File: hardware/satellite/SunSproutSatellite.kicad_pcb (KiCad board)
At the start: 4 copper layers, 27.2 x 51.1 mm, 36 parts, among them J1 RJHSE5380_QwiicBusCompatible, J2 Conn_01x03, J3 Conn_01x03, J4 Conn_01x03, J5 Conn_01x03, J6 Conn_01x03, J7 Conn_01x04, J8 Qwiic, U1 PCA9615DPZ, U2 ADS1115IDGS, U3 DS2482S-100+, U4 USBLC6-4SC6

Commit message: fix(satellite): Consolidate shared libraries, fix MDX/links, and update JST PA LCSC part (#24)
* Consolidate Hub and Satellite libraries into shared hardware/libraries

* Add SunSprout logo to Satellite silkscreen and refresh documentation assets

* Fix MDX compilation error and broken links in satellite documentation

* Update DS18B20 and moisture probe connectors to JST PA with LCSC part C131339
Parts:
- added G***: LOGO, project:Logo, B.Cu at (122.1, 113.2)
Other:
- board text added: "SunSproutSatellite REV ${REV_NUM}(${VCSSHORTHASH})"

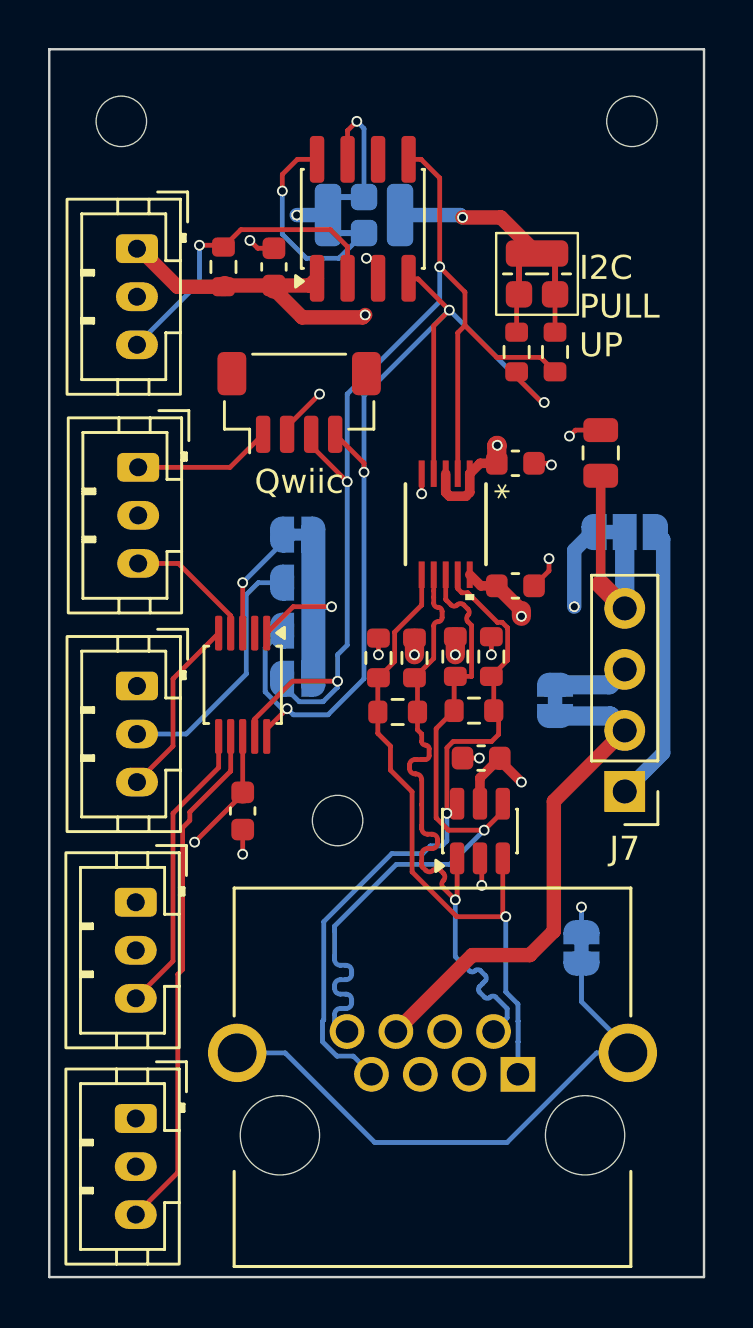
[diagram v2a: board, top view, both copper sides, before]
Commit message: feat(hardware): complete satellite pcb routing and layout review fixes
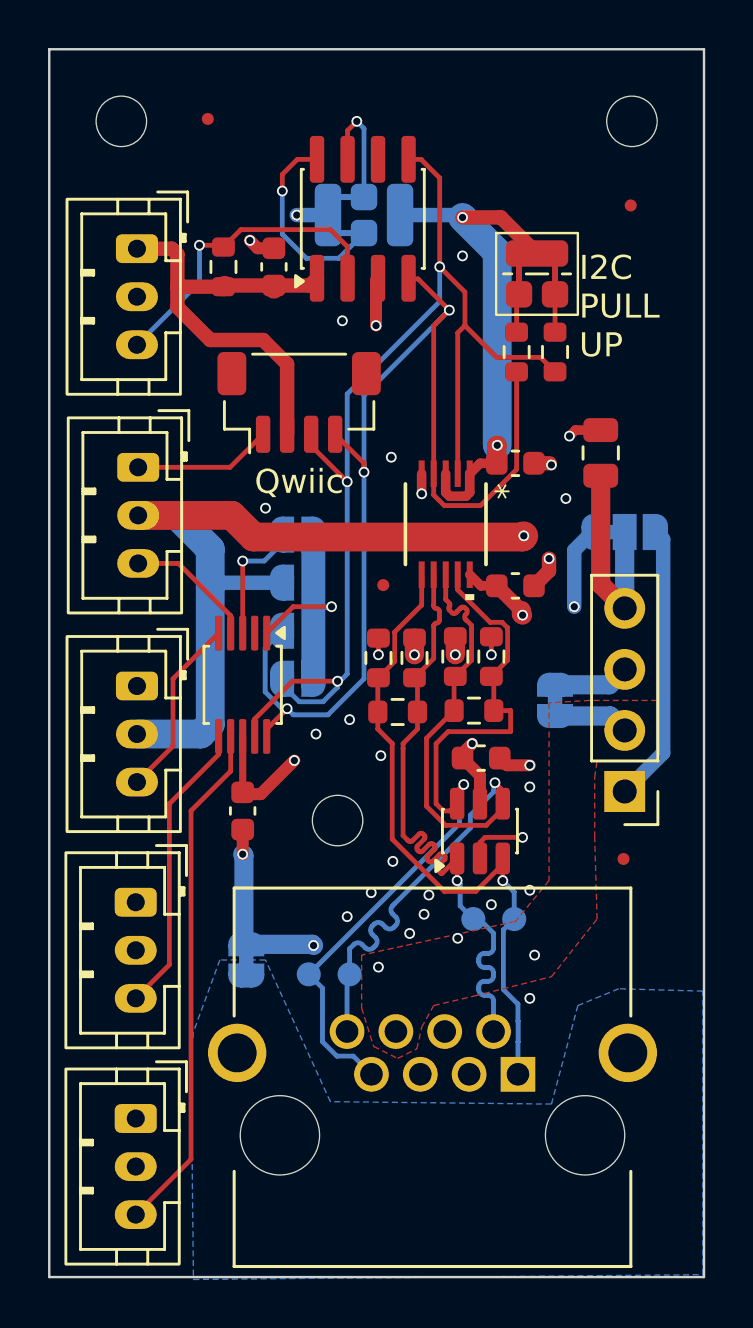
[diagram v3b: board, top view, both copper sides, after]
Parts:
- added Ref**: Fiducial_0.5mm_Mask1mm, PCM_SparkFun-Aesthetic:Fiducial_0.5mm_Mask1mm, F.Cu at (113.9, 122.3)
- added Ref**: Fiducial_0.5mm_Mask1mm, PCM_SparkFun-Aesthetic:Fiducial_0.5mm_Mask1mm, F.Cu at (106.6, 102.9)
- added Ref**: Fiducial_0.5mm_Mask1mm, PCM_SparkFun-Aesthetic:Fiducial_0.5mm_Mask1mm, F.Cu at (123.9, 133.7)
- added Ref**: Fiducial_0.5mm_Mask1mm, PCM_SparkFun-Aesthetic:Fiducial_0.5mm_Mask1mm, F.Cu at (124.2, 106.5)
- added TP4: TestPoint_2Pole, project:TestPoint_2Pole_Pad_D1.0mm, B.Cu at (118.5, 136.2)
- added TP5: TestPoint_2Pole, project:TestPoint_2Pole_Pad_D1.0mm, B.Cu at (111.7, 138.5)
- moved JP13 14.0 mm to (108.2, 137.9)
- moved G*** 3.90 mm to (122.1, 109.3)
- turned C6 to 0 degrees
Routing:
- net VCC_2: track 38.7 -> 13.2 mm
- net SHIELD: track 24.0 -> 0.00 mm
- net GND_2: track 21.0 -> 3.15 mm
- net SAT_3V3: track 153.3 -> 170.0 mm, vias 9 -> 8
- net GND: track 27.1 -> 36.6 mm, vias 14 -> 35
- net DSDA_N: track 29.2 -> 32.9 mm
- net SCL_LOCAL: track 45.0 -> 46.9 mm, vias 4 -> 3
- net DSDA_P: track 30.1 -> 31.8 mm
- net DSCL_P: track 26.8 -> 27.6 mm
- added copper zone on In2.Cu, net GND
- added copper zone on F.Cu, net GND_2
- added copper zone on B.Cu, net SHIELD
- added copper zone on In2.Cu, net VCC_2
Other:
- board text added: "+"
- board text added: "DSCL"
- board text added: "DSDA"
- board text added: "JP_VCC"
